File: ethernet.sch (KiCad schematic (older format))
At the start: 32 parts

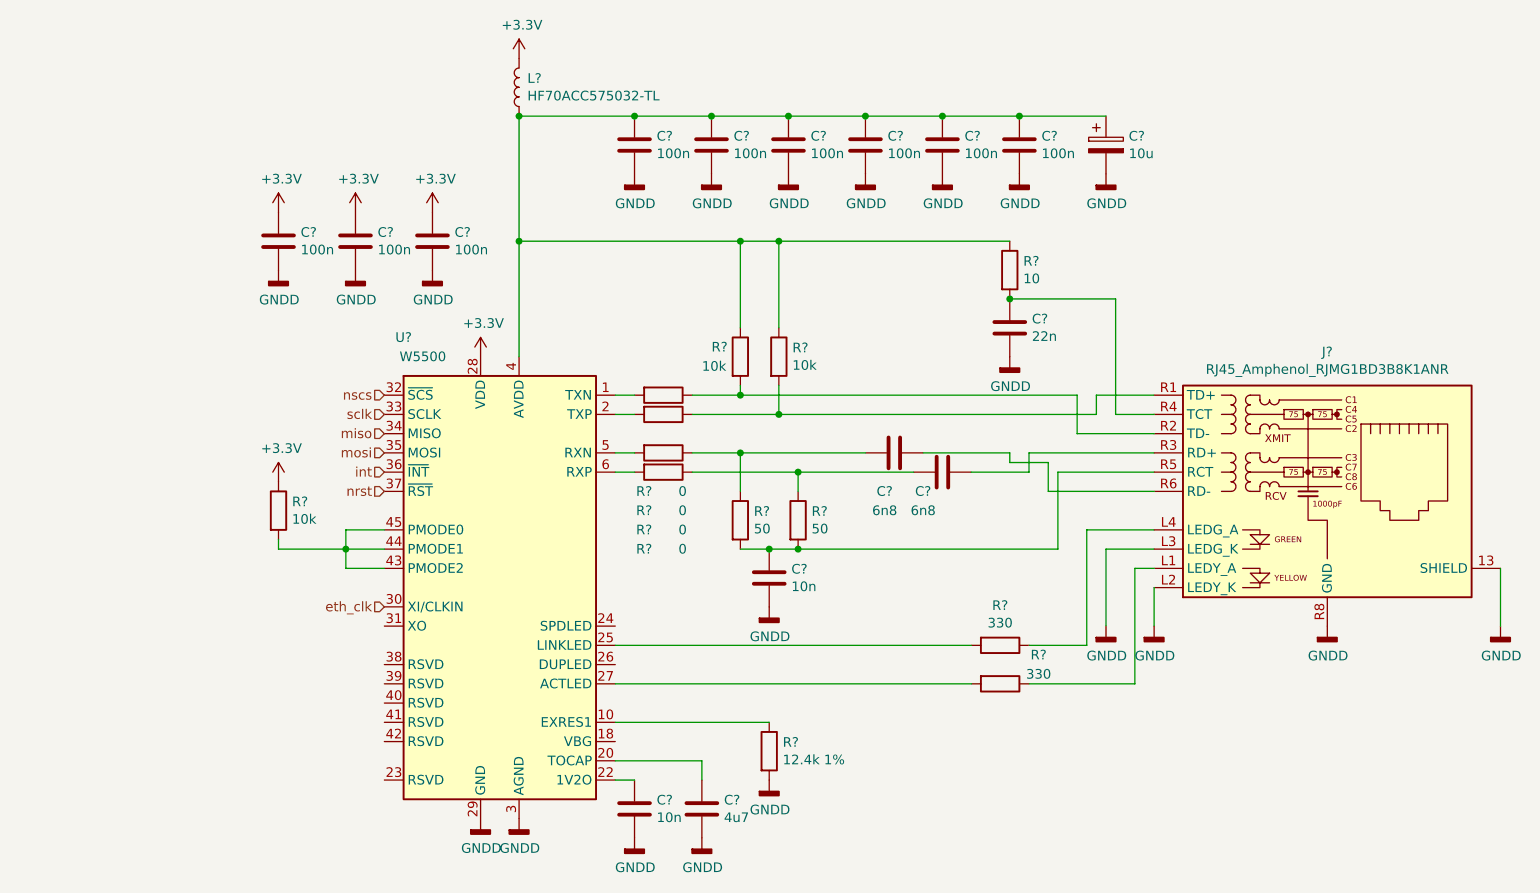
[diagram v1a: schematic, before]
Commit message: correct  op amp type to rail-to-rail
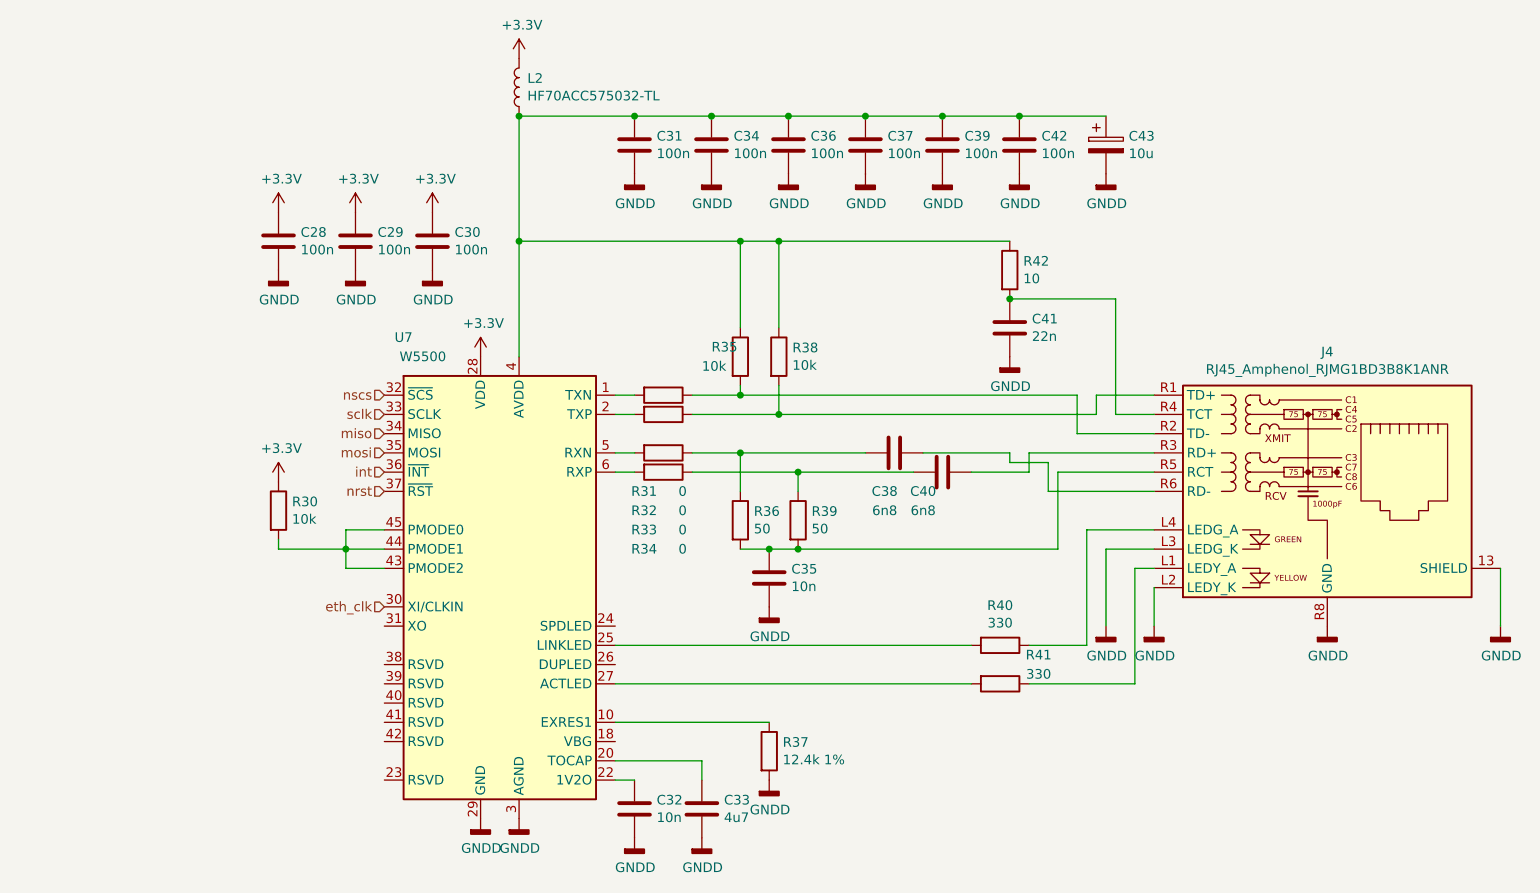
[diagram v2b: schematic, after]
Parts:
- gave numbers to parts that had none: 32

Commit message: ++
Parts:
- removed R30: 10k, symbol Device:R
- added C16, C18: 18p, Capacitor_SMD:C_0805_2012Metric_Pad1.18x1.45mm_HandSolder, symbol Device:C
- added R31: 1M, Resistor_SMD:R_0805_2012Metric_Pad1.20x1.40mm_HandSolder, symbol Device:R
- added Y2: 25MHz, Crystal:Crystal_HC18-U_Vertical, symbol Device:Crystal
- C17: renamed from C28; footprint (none) -> Capacitor_SMD:C_0805_2012Metric_Pad1.18x1.45mm_HandSolder
- C19: renamed from C29; footprint (none) -> Capacitor_SMD:C_0805_2012Metric_Pad1.18x1.45mm_HandSolder
- C20: renamed from C30; footprint (none) -> Capacitor_SMD:C_0805_2012Metric_Pad1.18x1.45mm_HandSolder
- C21: renamed from C31; footprint (none) -> Capacitor_SMD:C_0805_2012Metric_Pad1.18x1.45mm_HandSolder
- C22: renamed from C32; footprint (none) -> Capacitor_SMD:C_0805_2012Metric_Pad1.18x1.45mm_HandSolder
- C23: renamed from C33; footprint (none) -> Capacitor_SMD:C_1206_3216Metric_Pad1.33x1.80mm_HandSolder
- C24: renamed from C34; footprint (none) -> Capacitor_SMD:C_0805_2012Metric_Pad1.18x1.45mm_HandSolder
- C25: renamed from C35; footprint (none) -> Capacitor_SMD:C_0805_2012Metric_Pad1.18x1.45mm_HandSolder
- C26: renamed from C36; footprint (none) -> Capacitor_SMD:C_0805_2012Metric_Pad1.18x1.45mm_HandSolder
- C27: renamed from C37; footprint (none) -> Capacitor_SMD:C_0805_2012Metric_Pad1.18x1.45mm_HandSolder
- C28: renamed from C38; footprint (none) -> Capacitor_SMD:C_0805_2012Metric_Pad1.18x1.45mm_HandSolder
- C29: renamed from C39; footprint (none) -> Capacitor_SMD:C_0805_2012Metric_Pad1.18x1.45mm_HandSolder
- C30: renamed from C40; footprint (none) -> Capacitor_SMD:C_0805_2012Metric_Pad1.18x1.45mm_HandSolder
- C31: renamed from C41; footprint (none) -> Capacitor_SMD:C_0805_2012Metric_Pad1.18x1.45mm_HandSolder
- C32: renamed from C42; footprint (none) -> Capacitor_SMD:C_0805_2012Metric_Pad1.18x1.45mm_HandSolder
- C33: renamed from C43; footprint (none) -> Capacitor_THT:CP_Radial_D5.0mm_P2.00mm
- L1: renamed from L2; footprint (none) -> Inductor_SMD:L_0805_2012Metric_Pad1.15x1.40mm_HandSolder
- R33: renamed from R31; footprint (none) -> Resistor_SMD:R_0805_2012Metric_Pad1.20x1.40mm_HandSolder
- R34: renamed from R32; footprint (none) -> Resistor_SMD:R_0805_2012Metric_Pad1.20x1.40mm_HandSolder
- R35: renamed from R33; footprint (none) -> Resistor_SMD:R_0805_2012Metric_Pad1.20x1.40mm_HandSolder
- R36: renamed from R34; footprint (none) -> Resistor_SMD:R_0805_2012Metric_Pad1.20x1.40mm_HandSolder
- R37: renamed from R35; footprint (none) -> Resistor_SMD:R_0805_2012Metric_Pad1.20x1.40mm_HandSolder
- R38: renamed from R36; footprint (none) -> Resistor_SMD:R_0805_2012Metric_Pad1.20x1.40mm_HandSolder
- R39: renamed from R37; footprint (none) -> Resistor_SMD:R_0805_2012Metric_Pad1.20x1.40mm_HandSolder
- R40: renamed from R38; footprint (none) -> Resistor_SMD:R_0805_2012Metric_Pad1.20x1.40mm_HandSolder
- R41: renamed from R39; footprint (none) -> Resistor_SMD:R_0805_2012Metric_Pad1.20x1.40mm_HandSolder
- R42: renamed from R40; footprint (none) -> Resistor_SMD:R_0805_2012Metric_Pad1.20x1.40mm_HandSolder
- R43: renamed from R41; footprint (none) -> Resistor_SMD:R_0805_2012Metric_Pad1.20x1.40mm_HandSolder
- R44: renamed from R42; footprint (none) -> Resistor_SMD:R_0805_2012Metric_Pad1.20x1.40mm_HandSolder
- renumbered J4 to J3, U7 to U5
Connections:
- net GNDD: now also U5.43 (PMODE2), U5.44 (PMODE1), U5.45 (PMODE0), C16.2, C18.2
- net at U5.31 (XO): now also C16.1, R31.2, Y2.1
- net eth_clk: no longer names the net of U5.30 (XI/CLKIN)
- net eth_clk: now also C18.1, R31.1, Y2.2

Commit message: Bottom silk
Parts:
- J3: value RJ45_Amphenol_RJMG1BD3B8K1ANR -> RB1-1D6B8K1A
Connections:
- no-connect marks 0 -> 9
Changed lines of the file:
@@
 P 9000 3200
 F 0 "J3" H 9000 3925 50  0000 C CNN
-F 1 "RJ45_Amphenol_RJMG1BD3B8K1ANR" H 9000 3834 50  0000 C CNN
+F 1 "RB1-1D6B8K1A" H 9000 3834 50  0000 C CNN
 F 2 "Connector_RJ:RJ45_Amphenol_RJMG1BD3B8K1ANR" H 9000 3900 50  0001 C CNN
 F 3 "https://www.amphenolcanada.com/ProductSearch/Drawings/AC/RJMG1BD3B8K1ANR.PDF" H 9000 4000 50  0001 C CNN
@@
 	1    0    0    -1
 $EndComp
+NoConn ~ 4100 4700
+NoConn ~ 4100 4500
+NoConn ~ 4100 4400
+NoConn ~ 4100 4300
+NoConn ~ 4100 4200
+NoConn ~ 4100 4100
+NoConn ~ 5300 4500
+NoConn ~ 5300 4100
+NoConn ~ 5300 3900
 $EndSCHEMATC
